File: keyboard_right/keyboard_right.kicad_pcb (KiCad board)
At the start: 2 copper layers, 174 x 144 mm, 39 parts, among them J1 AudioJack4, SW1 SW_MEC_5G, SW10 SW_MEC_5G, SW11 SW_MEC_5G, SW12 SW_MEC_5G, SW13 SW_MEC_5G, SW14 SW_MEC_5G, SW15 SW_MEC_5G, SW16 SW_MEC_5G, SW17 SW_MEC_5G, SW18 SW_MEC_5G, SW19 SW_MEC_5G, SW2 SW_MEC_5G, SW20 SW_MEC_5G, SW21 SW_MEC_5G, SW22 SW_MEC_5G, SW23 SW_MEC_5G, SW24 SW_MEC_5G, SW25 SW_MEC_5G, SW26 SW_MEC_5G, SW27 SW_MEC_5G, SW28 SW_MEC_5G, SW29 SW_MEC_5G, SW3 SW_MEC_5G, SW30 SW_MEC_5G, SW31 SW_MEC_5G, SW32 SW_MEC_5G, SW4 SW_MEC_5G, SW5 SW_MEC_5G, SW6 SW_MEC_5G, SW7 SW_MEC_5G, SW8 SW_MEC_5G, SW9 SW_MEC_5G, U1 MCP23017-E_SO, U2 MCP23017-E_SO

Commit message: MageV2: Added V2.0 Right Side Board
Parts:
- R3, R4, U1, U2: moved to F.Cu
- SW29: footprint Switch_Keyboard_Kailh:SW_Kailh_Choc_V1V2_1.50u_90deg -> Switch_Keyboard_Kailh:SW_Kailh_Choc_V1V2_1.00u
- moved U1 47.0 mm to (173.4, 40.0), turned to 90 degrees
- moved SW29 27.6 mm to (83.0, 135.0), turned to -30 degrees
- moved SW30 27.6 mm to (84.0, 162.0)
- moved SW31 27.6 mm to (97.0, 149.0)
- moved SW32 27.6 mm to (112.0, 159.0)
- moved R4 22.7 mm to (119.4, 36.0), turned to -90 degrees
- moved R2 16.1 mm to (94.9, 37.0), turned to -90 degrees
- moved J1 12.0 mm to (87.3, 41.0)
- moved R1 11.1 mm to (95.0, 44.6)
- moved U2 6.53 mm to (108.0, 40.0), turned to 90 degrees
- moved R3 4.32 mm to (124.0, 36.0), turned to -90 degrees
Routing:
- net /Reset 1: track 2.52 -> 54.5 mm
- net /SDA: track 78.1 -> 127.0 mm, vias 1 -> 0
- net /SCK: track 66.9 -> 113.0 mm, vias 1 -> 0
- net Net-(SW8-Pad2): track 119.0 -> 73.0 mm
- net Net-(SW6-Pad2): track 86.1 -> 41.5 mm
- net Net-(SW7-Pad2): track 103.4 -> 59.0 mm
- net Net-(SW5-Pad2): track 68.9 -> 25.4 mm
- net Net-(SW2-Pad2): track 108.7 -> 66.2 mm
- net Net-(SW3-Pad2): track 124.9 -> 83.2 mm
- net Net-(SW4-Pad2): track 141.7 -> 101.3 mm
- net Net-(SW1-Pad2): track 90.0 -> 50.8 mm
- net Net-(SW11-Pad2): track 92.6 -> 65.3 mm
- net Net-(SW12-Pad2): track 114.3 -> 87.2 mm
- net Net-(SW10-Pad2): track 75.4 -> 48.3 mm
- net Net-(SW9-Pad2): track 55.6 -> 29.8 mm
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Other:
- board size 174 x 144 mm -> 146 x 145 mm
- board text added: "MageV2 by mosswg"
- board text removed: "5V"

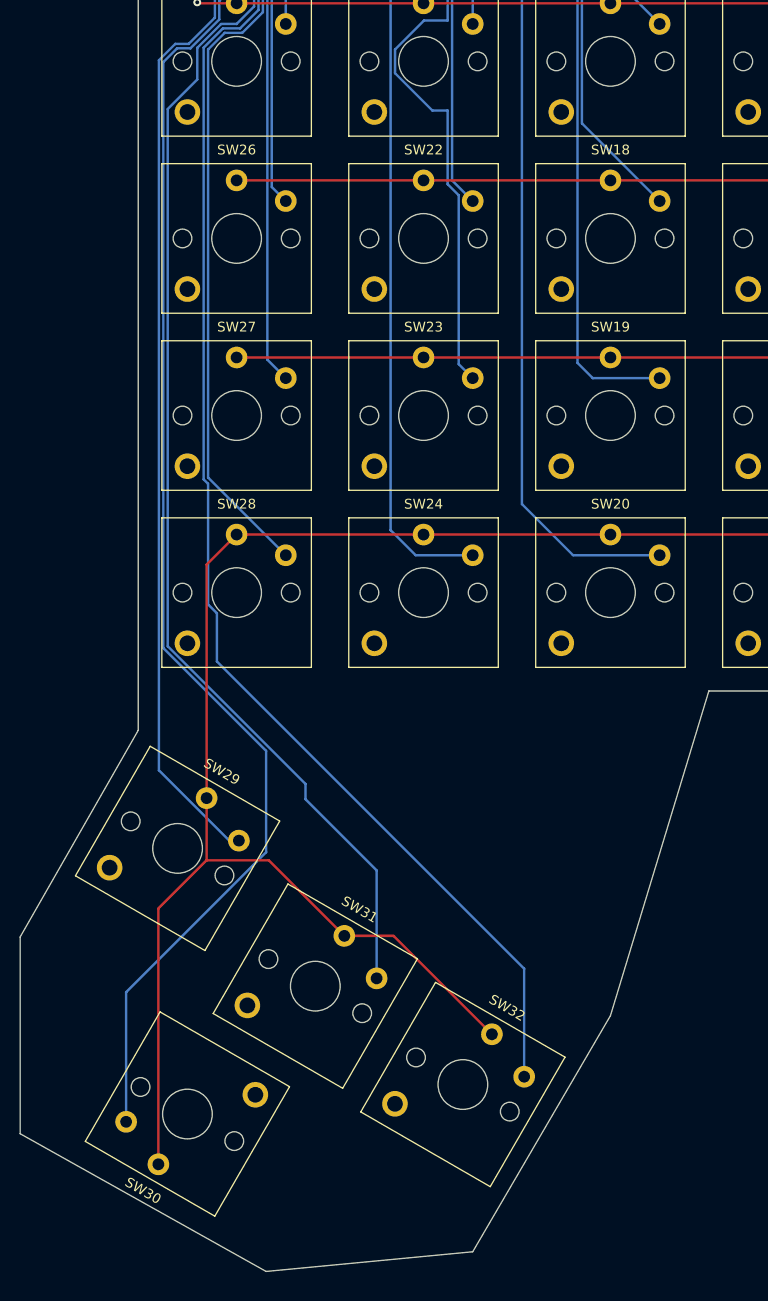
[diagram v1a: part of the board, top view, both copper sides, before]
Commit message: MageV2.1 Left: Modified the Thumb Control Cluster
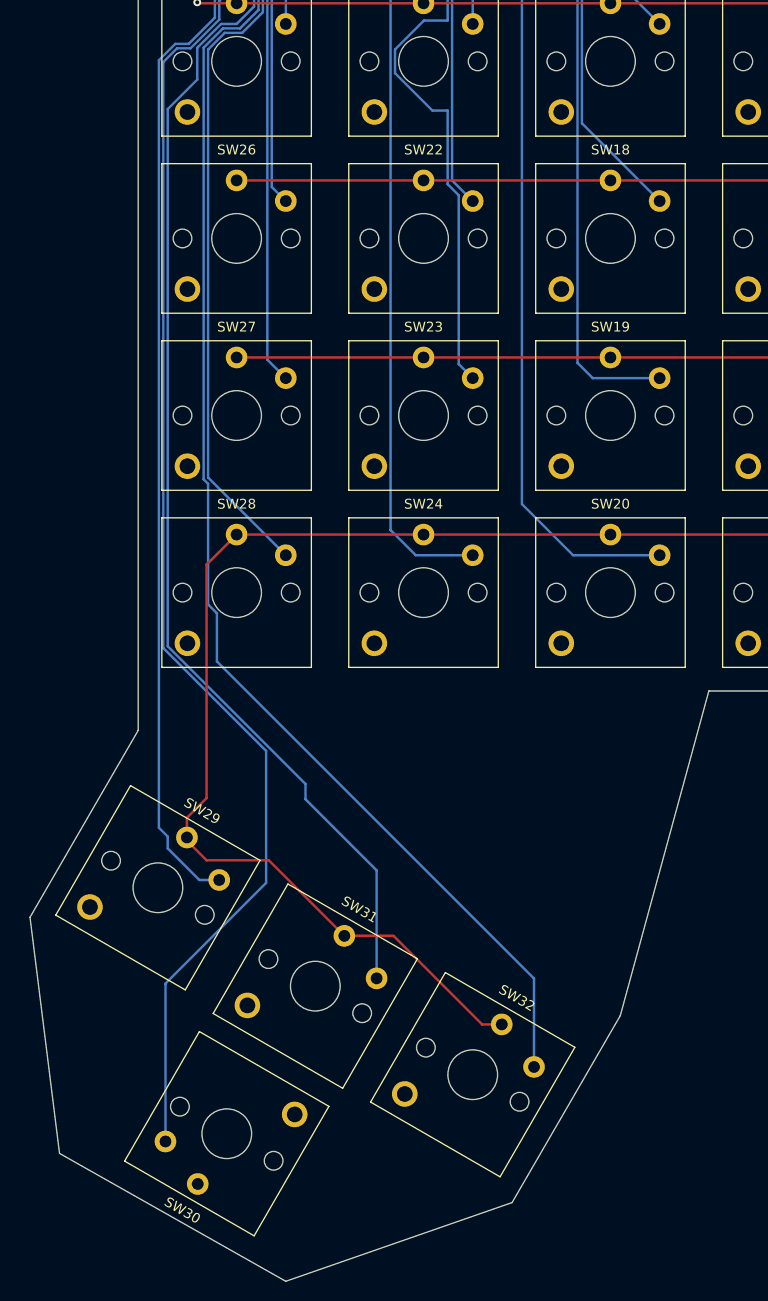
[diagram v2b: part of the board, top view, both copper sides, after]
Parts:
- SW32: footprint Switch_Keyboard_Kailh:SW_Kailh_Choc_V1V2_1.50u_90deg -> Switch_Keyboard_Kailh:SW_Kailh_Choc_V1V2_1.00u
- moved SW29 4.47 mm to (81.0, 139.0)
- moved SW30 4.47 mm to (88.0, 164.0)
- moved SW32 1.41 mm to (113.0, 158.0)
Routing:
- net +5V: track 741.7 -> 711.0 mm
- net Net-(SW29-Pad2): track 119.2 -> 123.0 mm
- net Net-(SW32-Pad2): track 143.3 -> 142.7 mm
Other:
- board size 146 x 145 mm -> 145 x 146 mm
